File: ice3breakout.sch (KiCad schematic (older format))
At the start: 15 parts, among them CON1 AVR-ISP-6, CON2 AVR-JTAG-10, CON3 AVR-PDI-6, CON4 USB-MICRO-B, P1 Jtag ICE3, P2 Cortex M0 debug, P3 ice3 expansion, P4 Supply select, SW1 SW_PUSH, U1 AP1117D33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

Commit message: Added schematic as pdf, and manufacturing files
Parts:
- added P5: Supply, Pin_Headers:Pin_Header_Straight_1x02, symbol CONN_01X02
- added P6: GND, Pin_Headers:Pin_Header_Straight_1x01, symbol CONN_01X01
- U1, U2: footprint Housings_SOT-89:SOT89-3_Housing_Handsoldering -> SMD_Packages:SOT-223
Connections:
- net +5V: now also P5.1 (P1)
- net GND: now also P1.10 (P10), P3.10 (P10), P5.2 (P2), P6.1 (P1)
- net RST: now also CON2.6, CON3.5
- net at CON1.1, CON2.3, P1.3 (P3)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: now also CON3.1
- no-connect marks 6 -> 12
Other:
- moved on the sheet: CON3

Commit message: Added pin legend to silkscreen, OSHW logo to bottom layer copper
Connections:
- net at CON1.1, CON2.3, CON3.1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: now also P2.6 (P6)
- net at CON1.4, CON2.9, P1.9 (P9)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: now also P2.8 (P8)
- no-connect marks 12 -> 10
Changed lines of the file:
@@
-$EndComp
-$Comp
-L Debug P2
-U 1 1 55C252B4
-P 2550 5300
-F 0 "P2" H 2550 5600 50  0000 C CNN
-F 1 "Cortex M0 debug" H 2550 5000 50  0000 C CNN
-F 2 "mysensors_connectors:FCI_10P_HDR" H 2550 4100 60  0001 C CNN
-F 3 "" H 2550 4100 60  0000 C CNN
-F 4 "FCI" H 2550 5300 60  0001 C CNN "Vendor"
-F 5 "Mouser" H 2550 5300 60  0001 C CNN "Supplier1"
-F 6 "649-221511-00010T4LF" H 2550 5300 60  0001 C CNN "Supplier1 part"
-F 7 "20021511-00010T4LF" H 2550 5300 60  0001 C CNN "Vendor part"
-F 8 "Digikey" H 2550 5300 60  0001 C CNN "Supplier2"
-	1    2550 5300
-	1    0    0    -1
 $EndComp
 $Comp
@@
 	2300 3650 2000 3650
 Wire Wire Line
-	2000 2400 2000 4550
+	2000 2400 2000 4900
 Wire Wire Line
 	2000 4550 2300 4550
@@
 	2150 4250 2300 4250
 Wire Wire Line
-	2150 1250 2150 4250
+	2150 1250 2150 4850
 Wire Wire Line
 	2150 3350 2300 3350
@@
 Connection ~ 2200 4150
 NoConn ~ 2300 5500
-NoConn ~ 2800 5300
-NoConn ~ 2800 5400
 Wire Wire Line
 	2400 2400 2000 2400
@@
 07 00 85 88 3B 00 28 44 DC 01 40 21 E2 0E 00 0A 11 77 00 50 88 B8 03 80 42 C4 1D 00 14 22 EE 00
 A0 10 71 07 00 85 88 3B 00 28 F4 2F 6E 0E 73 66 69 F5 31 42 00 00 00 00 49 45 4E 44 AE 42 60 82
-78
+A0
 EndData
 $EndBitmap
+$Comp
+L Debug P2
+U 1 1 55C252B4
+P 2550 5300
+F 0 "P2" H 2550 5600 50  0000 C CNN
+F 1 "Cortex M0 debug" H 2550 5000 50  0000 C CNN
+F 2 "mysensors_connectors:FCI_10P_HDR" H 2550 4100 60  0001 C CNN
+F 3 "" H 2550 4100 60  0000 C CNN
+F 4 "FCI" H 2550 5300 60  0001 C CNN "Vendor"
+F 5 "Mouser" H 2550 5300 60  0001 C CNN "Supplier1"
+F 6 "649-221511-00010T4LF" H 2550 5300 60  0001 C CNN "Supplier1 part"
+F 7 "20021511-00010T4LF" H 2550 5300 60  0001 C CNN "Vendor part"
+F 8 "Digikey" H 2550 5300 60  0001 C CNN "Supplier2"
+	1    2550 5300
+	1    0    0    -1
+$EndComp
+Wire Wire Line
+	2150 4850 3050 4850
+Wire Wire Line
+	3050 4850 3050 5300
+Wire Wire Line
+	3050 5300 2800 5300
+Connection ~ 2150 4250
+Wire Wire Line
+	2000 4900 3100 4900
+Wire Wire Line
+	3100 4900 3100 5400
+Wire Wire Line
+	3100 5400 2800 5400
+Connection ~ 2000 4550
 $EndSCHEMATC

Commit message: closes #1, closes #2, closes #3
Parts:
- removed CON3: AVR-PDI-6, w_conn_strip:vasch_strip_3x2, symbol AVR-PDI-6
- added C4: C, Capacitors_SMD:C_0603_HandSoldering, symbol C
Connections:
- net +1V8: now also C4.1; no longer C3.1
- net +3V3: no longer U2.3 (VI)
- net +5V: now also C3.1, U2.3 (VI)
- net GND: now also C4.2
- no-connect marks 10 -> 8
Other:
- moved on the sheet: C3, U2
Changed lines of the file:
@@
-$EndComp
-$Comp
-L AVR-PDI-6 CON3
-U 1 1 55C24911
-P 2500 1350
-F 0 "CON3" H 2420 1590 50  0000 C CNN
-F 1 "AVR-PDI-6" H 2290 1105 50  0000 L BNN
-F 2 "w_conn_strip:vasch_strip_3x2" V 2055 1385 50  0001 C CNN
-F 3 "" H 2500 1350 60  0000 C CNN
-	1    2500 1350
-	1    0    0    -1
 $EndComp
 $Comp
@@
 	5550 5450 5550 5250
 Wire Wire Line
-	2300 3650 2000 3650
+	2000 3650 2300 3650
 Wire Wire Line
 	2000 2400 2000 4900
@@
 	2150 4250 2300 4250
 Wire Wire Line
-	2150 1250 2150 4850
-Wire Wire Line
 	2150 3350 2300 3350
 Wire Wire Line
-	2300 3250 2200 3250
+	2200 3250 2300 3250
 Wire Wire Line
 	2200 2000 2200 4800
@@
 Wire Wire Line
 	3100 2700 3100 2200
-Wire Wire Line
-	2650 2200 3350 2200
-$Comp
-L GND #PWR010
-U 1 1 55C31CFB
-P 2900 1550
-F 0 "#PWR010" H 2900 1300 50  0001 C CNN
-F 1 "GND" H 2900 1400 50  0000 C CNN
-F 2 "" H 2900 1550 60  0000 C CNN
-F 3 "" H 2900 1550 60  0000 C CNN
-	1    2900 1550
-	1    0    0    -1
-$EndComp
-Wire Wire Line
-	2900 1550 2900 1450
-Wire Wire Line
-	2900 1450 2650 1450
-$Comp
-L VCC #PWR011
-U 1 1 55C31D7B
-P 2900 1000
-F 0 "#PWR011" H 2900 850 50  0001 C CNN
-F 1 "VCC" H 2900 1150 50  0000 C CNN
-F 2 "" H 2900 1000 60  0000 C CNN
-F 3 "" H 2900 1000 60  0000 C CNN
-	1    2900 1000
-	1    0    0    -1
-$EndComp
-Wire Wire Line
-	2900 1000 2900 1250
-Wire Wire Line
-	2900 1250 2650 1250
-NoConn ~ 2650 1350
-NoConn ~ 2350 1350
 $Comp
 L AP1117D18 U2
 U 1 1 55C33EF0
-P 6700 4250
-F 0 "U2" H 6800 4000 50  0000 C CNN
-F 1 "AP1117D18" H 6700 4500 50  0000 C CNN
-F 2 "SMD_Packages:SOT-223" H 6700 4250 60  0001 C CNN
-F 3 "" H 6700 4250 60  0000 C CNN
-	1    6700 4250
+P 6950 4250
+F 0 "U2" H 7050 4000 50  0000 C CNN
+F 1 "AP1117D18" H 6950 4500 50  0000 C CNN
+F 2 "SMD_Packages:SOT-223" H 6950 4250 60  0001 C CNN
+F 3 "" H 6950 4250 60  0000 C CNN
+	1    6950 4250
 	1    0    0    -1
 $EndComp
@@
 $EndComp
 $Comp
-L GND #PWR012
+L GND #PWR010
 U 1 1 55C33FBB
 P 6300 4750
-F 0 "#PWR012" H 6300 4500 50  0001 C CNN
+F 0 "#PWR010" H 6300 4500 50  0001 C CNN
 F 1 "GND" H 6300 4600 50  0000 C CNN
 F 2 "" H 6300 4750 60  0000 C CNN
@@
 	5900 4550 5900 4750
 Wire Wire Line
-	5450 4750 7050 4750
-Wire Wire Line
-	6700 4750 6700 4550
+	5450 4750 7300 4750
+Wire Wire Line
+	6950 4750 6950 4550
 Connection ~ 6300 4750
 $Comp
@@
 $EndComp
 $Comp
-L GND #PWR013
+L GND #PWR011
 U 1 1 55C34110
 P 6450 5950
-F 0 "#PWR013" H 6450 5700 50  0001 C CNN
+F 0 "#PWR011" H 6450 5700 50  0001 C CNN
 F 1 "GND" H 6450 5800 50  0000 C CNN
 F 2 "" H 6450 5950 60  0000 C CNN
@@
 $EndComp
 $Comp
-L +5V #PWR014
+L +5V #PWR012
 U 1 1 55C3412F
 P 6450 5250
-F 0 "#PWR014" H 6450 5100 50  0001 C CNN
+F 0 "#PWR012" H 6450 5100 50  0001 C CNN
 F 1 "+5V" H 6450 5390 50  0000 C CNN
 F 2 "" H 6450 5250 60  0000 C CNN
@@
 	6450 5800 6500 5800
 $Comp
-L +3V3 #PWR015
+L +3V3 #PWR013
 U 1 1 55C34259
-P 6200 3900
-F 0 "#PWR015" H 6200 3750 50  0001 C CNN
-F 1 "+3V3" H 6200 4040 50  0000 C CNN
-F 2 "" H 6200 3900 60  0000 C CNN
-F 3 "" H 6200 3900 60  0000 C CNN
-	1    6200 3900
-	1    0    0    -1
-$EndComp
-$Comp
-L +1V8 #PWR016
+P 6300 3900
+F 0 "#PWR013" H 6300 3750 50  0001 C CNN
+F 1 "+3V3" H 6300 4040 50  0000 C CNN
+F 2 "" H 6300 3900 60  0000 C CNN
+F 3 "" H 6300 3900 60  0000 C CNN
+	1    6300 3900
+	1    0    0    -1
+$EndComp
+$Comp
+L +1V8 #PWR014
 U 1 1 55C34278
-P 7050 3900
-F 0 "#PWR016" H 7050 3750 50  0001 C CNN
-F 1 "+1V8" H 7050 4040 50  0000 C CNN
-F 2 "" H 7050 3900 60  0000 C CNN
-F 3 "" H 7050 3900 60  0000 C CNN
-	1    7050 3900
-	1    0    0    -1
-$EndComp
-Wire Wire Line
-	7050 3900 7050 4350
-Wire Wire Line
-	7050 4250 7000 4250
-Wire Wire Line
-	6200 4250 6200 3900
-Wire Wire Line
-	6200 4250 6400 4250
-$Comp
-L +5V #PWR017
+P 7300 3900
+F 0 "#PWR014" H 7300 3750 50  0001 C CNN
+F 1 "+1V8" H 7300 4040 50  0000 C CNN
+F 2 "" H 7300 3900 60  0000 C CNN
+F 3 "" H 7300 3900 60  0000 C CNN
+	1    7300 3900
+	1    0    0    -1
+$EndComp
+Wire Wire Line
+	7300 3900 7300 4350
+Wire Wire Line
+	7300 4250 7250 4250
+$Comp
+L +5V #PWR015
 U 1 1 55C343F3
 P 5450 3900
-F 0 "#PWR017" H 5450 3750 50  0001 C CNN
+F 0 "#PWR015" H 5450 3750 50  0001 C CNN
 F 1 "+5V" H 5450 4040 50  0000 C CNN
 F 2 "" H 5450 3900 60  0000 C CNN
@@
 Connection ~ 8050 3250
 $Comp
-L VCC #PWR018
+L VCC #PWR016
 U 1 1 55C347BD
 P 8050 2950
-F 0 "#PWR018" H 8050 2800 50  0001 C CNN
+F 0 "#PWR016" H 8050 2800 50  0001 C CNN
 F 1 "VCC" H 8050 3100 50  0000 C CNN
 F 2 "" H 8050 2950 60  0000 C CNN
@@
 Connection ~ 8050 3150
 $Comp
-L +1V8 #PWR019
+L +1V8 #PWR017
 U 1 1 55C34859
 P 7500 3050
-F 0 "#PWR019" H 7500 2900 50  0001 C CNN
+F 0 "#PWR017" H 7500 2900 50  0001 C CNN
 F 1 "+1V8" H 7500 3190 50  0000 C CNN
 F 2 "" H 7500 3050 60  0000 C CNN
@@
 $EndComp
 $Comp
-L +3V3 #PWR020
+L +3V3 #PWR018
 U 1 1 55C34879
 P 7300 3050
-F 0 "#PWR020" H 7300 2900 50  0001 C CNN
+F 0 "#PWR018" H 7300 2900 50  0001 C CNN
 F 1 "+3V3" H 7300 3190 50  0000 C CNN
 F 2 "" H 7300 3050 60  0000 C CNN
@@
 $EndComp
 $Comp
-L +5V #PWR021
+L +5V #PWR019
 U 1 1 55C34899
 P 7100 3050
-F 0 "#PWR021" H 7100 2900 50  0001 C CNN
+F 0 "#PWR019" H 7100 2900 50  0001 C CNN
 F 1 "+5V" H 7100 3190 50  0000 C CNN
 F 2 "" H 7100 3050 60  0000 C CNN
@@
 L C C3
 U 1 1 55C34A7C
-P 7050 4500
-F 0 "C3" H 7075 4600 50  0000 L CNN
-F 1 "C" H 7075 4400 50  0000 L CNN
-F 2 "Capacitors_SMD:C_0603_HandSoldering" H 7088 4350 30  0001 C CNN
-F 3 "" H 7050 4500 60  0000 C CNN
-	1    7050 4500
+P 6600 4500
+F 0 "C3" H 6625 4600 50  0000 L CNN
+F 1 "C" H 6625 4400 50  0000 L CNN
+F 2 "Capacitors_SMD:C_0603_HandSoldering" H 6638 4350 30  0001 C CNN
+F 3 "" H 6600 4500 60  0000 C CNN
+	1    6600 4500
 	1    0    0    -1
 $EndComp
@@
 Connection ~ 5900 4750
 Wire Wire Line
-	6300 4350 6300 4250
-Connection ~ 6300 4250
+	6300 3900 6300 4350
 Wire Wire Line
 	6300 4650 6300 4750
 Wire Wire Line
-	7050 4750 7050 4650
-Connection ~ 6700 4750
-Connection ~ 7050 4250
+	7300 4750 7300 4650
+Connection ~ 6950 4750
+Connection ~ 7300 4250
 $Comp
 L CONN_01X01 P6
@@
 $EndComp
 $Comp
-L GND #PWR022
+L GND #PWR020
 U 1 1 55C3530F
 P 4900 6250
-F 0 "#PWR022" H 4900 6000 50  0001 C CNN
+F 0 "#PWR020" H 4900 6000 50  0001 C CNN
 F 1 "GND" H 4900 6100 50  0000 C CNN
 F 2 "" H 4900 6250 60  0000 C CNN
@@
 $EndComp
 $Comp
-L GND #PWR023
+L GND #PWR021
 U 1 1 55C3549F
 P 7700 4050
-F 0 "#PWR023" H 7700 3800 50  0001 C CNN
+F 0 "#PWR021" H 7700 3800 50  0001 C CNN
 F 1 "GND" H 7700 3900 50  0000 C CNN
 F 2 "" H 7700 4050 60  0000 C CNN
@@
 	7700 4000 7700 4050
 $Comp
-L +5V #PWR024
+L +5V #PWR022
 U 1 1 55C35555
 P 7700 3850
-F 0 "#PWR024" H 7700 3700 50  0001 C CNN
+F 0 "#PWR022" H 7700 3700 50  0001 C CNN
 F 1 "+5V" H 7700 3990 50  0000 C CNN
 F 2 "" H 7700 3850 60  0000 C CNN
@@
 Wire Wire Line
 	7700 3850 7700 3900
-Wire Wire Line
-	2150 1250 2350 1250
-Connection ~ 2150 2100
-Wire Wire Line
-	2350 1450 2350 1700
-Wire Wire Line
-	2350 1700 3350 1700
-Wire Wire Line
-	3350 1700 3350 2200
-Connection ~ 3100 2200
 Wire Wire Line
 	4900 6200 5250 6200
@@
 NoConn ~ 7500 5800
 $Comp
-L GND #PWR025
+L GND #PWR023
 U 1 1 55C372D3
 P 3100 4600
-F 0 "#PWR025" H 3100 4350 50  0001 C CNN
+F 0 "#PWR023" H 3100 4350 50  0001 C CNN
 F 1 "GND" H 3100 4450 50  0000 C CNN
 F 2 "" H 3100 4600 60  0000 C CNN
@@
 07 00 85 88 3B 00 28 44 DC 01 40 21 E2 0E 00 0A 11 77 00 50 88 B8 03 80 42 C4 1D 00 14 22 EE 00
 A0 10 71 07 00 85 88 3B 00 28 F4 2F 6E 0E 73 66 69 F5 31 42 00 00 00 00 49 45 4E 44 AE 42 60 82
-A0
+78
 EndData
 $EndBitmap
@@
 	3100 5400 2800 5400
 Connection ~ 2000 4550
+Wire Wire Line
+	2150 2100 2150 4850
+Wire Wire Line
+	3100 2200 2650 2200
+Wire Wire Line
+	6300 4250 6200 4250
+Connection ~ 6300 4250
+$Comp
+L C C4
+U 1 1 55C4C554
+P 7300 4500
+F 0 "C4" H 7325 4600 50  0000 L CNN
+F 1 "C" H 7325 4400 50  0000 L CNN
+F 2 "Capacitors_SMD:C_0603_HandSoldering" H 7338 4350 30  0001 C CNN
+F 3 "" H 7300 4500 60  0000 C CNN
+F 4 "Mouser" H 7300 4500 60  0001 C CNN "Supplier1"
+F 5 "Digikey" H 7300 4500 60  0001 C CNN "Supplier2"
+	1    7300 4500
+	1    0    0    -1
+$EndComp
+Wire Wire Line
+	6600 3900 6600 4350
+Wire Wire Line
+	6600 4250 6650 4250
+Wire Wire Line
+	6600 4650 6600 4750
+Connection ~ 6600 4750
+$Comp
+L +5V #PWR024
+U 1 1 55C4C83C
+P 6600 3900
+F 0 "#PWR024" H 6600 3750 50  0001 C CNN
+F 1 "+5V" H 6600 4040 50  0000 C CNN
+F 2 "" H 6600 3900 60  0000 C CNN
+F 3 "" H 6600 3900 60  0000 C CNN
+	1    6600 3900
+	1    0    0    -1
+$EndComp
+Connection ~ 6600 4250
 $EndSCHEMATC

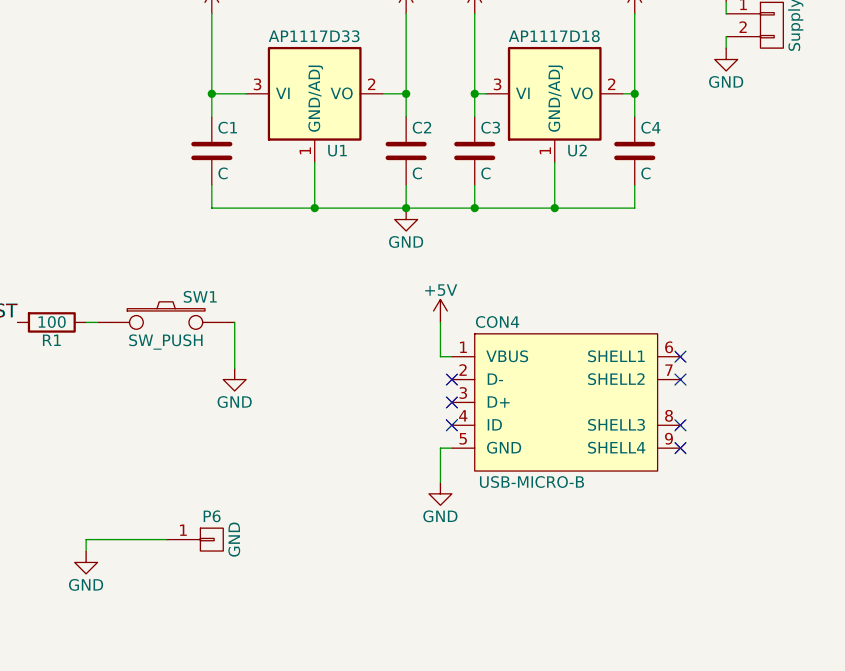
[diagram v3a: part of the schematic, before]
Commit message: Added extra GND pins
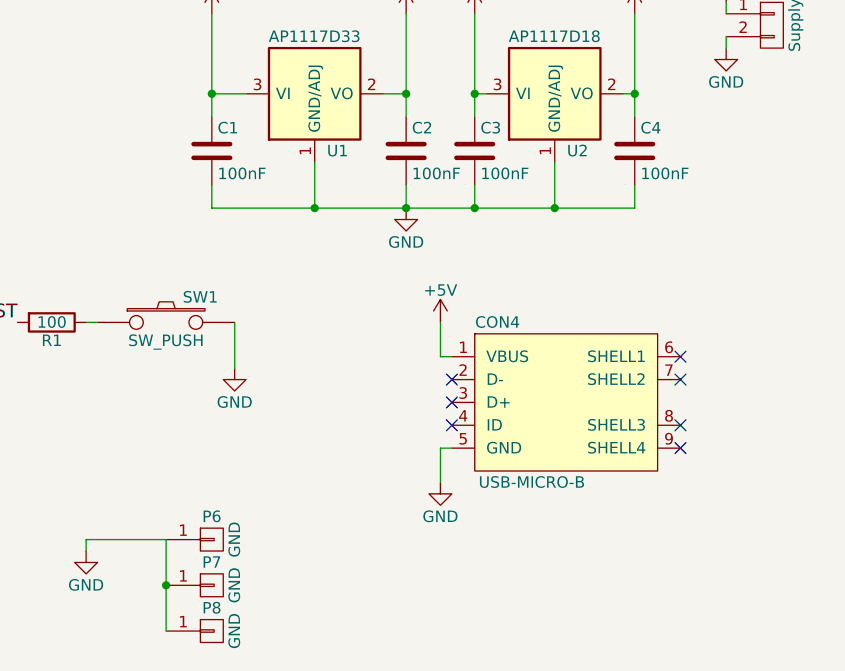
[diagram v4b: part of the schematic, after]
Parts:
- added P7, P8: GND, Pin_Headers:Pin_Header_Straight_1x01, symbol CONN_01X01
- C1, C2, C3: value C -> 100nF; Supplier1 (none) -> Mouser; Supplier1 part (none) -> 81-GRM39X104K16J; Supplier2 (none) -> Digikey; Vendor (none) -> Murata Electronics; Vendor part (none) -> GRM188R71C104KA01J
- C4: value C -> 100nF; Supplier1 part (none) -> 81-GRM39X104K16J; Vendor (none) -> Murata Electronics; Vendor part (none) -> GRM188R71C104KA01J
- CON1: Supplier1 (none) -> Mouser; Supplier1 part (none) -> 649-75869-131LF; Supplier2 (none) -> Digikey; Vendor (none) -> FCI; Vendor part (none) -> 75869-131LF
- CON2: Supplier1 (none) -> Mouser; Supplier1 part (none) -> 649-861312324345E1LF; Supplier2 (none) -> Digikey; Vendor (none) -> FCI; Vendor part (none) -> 86130102324345E1LF
- R1: Supplier1 (none) -> Mouser; Supplier1 part (none) -> 71-CRCW0603-100-E3; Supplier2 (none) -> Digikey; Vendor (none) -> Vishay; Vendor part (none) -> CRCW0603100RFKEA
- SW1: Supplier1 (none) -> Mouser; Supplier1 part (none) -> 506-147873-2; Supplier2 (none) -> Digikey; Vendor (none) -> TE Connectivity; Vendor part (none) -> 147873-2
- U1: Supplier1 (none) -> Mouser; Supplier1 part (none) -> 863-NCP1117ST33T3G; Supplier2 (none) -> Digikey; Vendor (none) -> ON Semiconductor; Vendor part (none) -> NCP1117ST33T3G
- U2: Supplier1 (none) -> Mouser; Supplier1 part (none) -> 863-NCP1117ST18T3G; Supplier2 (none) -> Digikey; Vendor (none) -> ON Semiconductor; Vendor part (none) -> NCP1117ST18T3G
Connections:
- net GND: now also P7.1 (P1), P8.1 (P1)
